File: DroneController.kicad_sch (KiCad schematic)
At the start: 36 parts, among them P1 USB_C_Plug, U2 TPS62152RGTR, U3 BMP280, U4 MPU-6500, U6 L86-M33, Y1 8Mhz

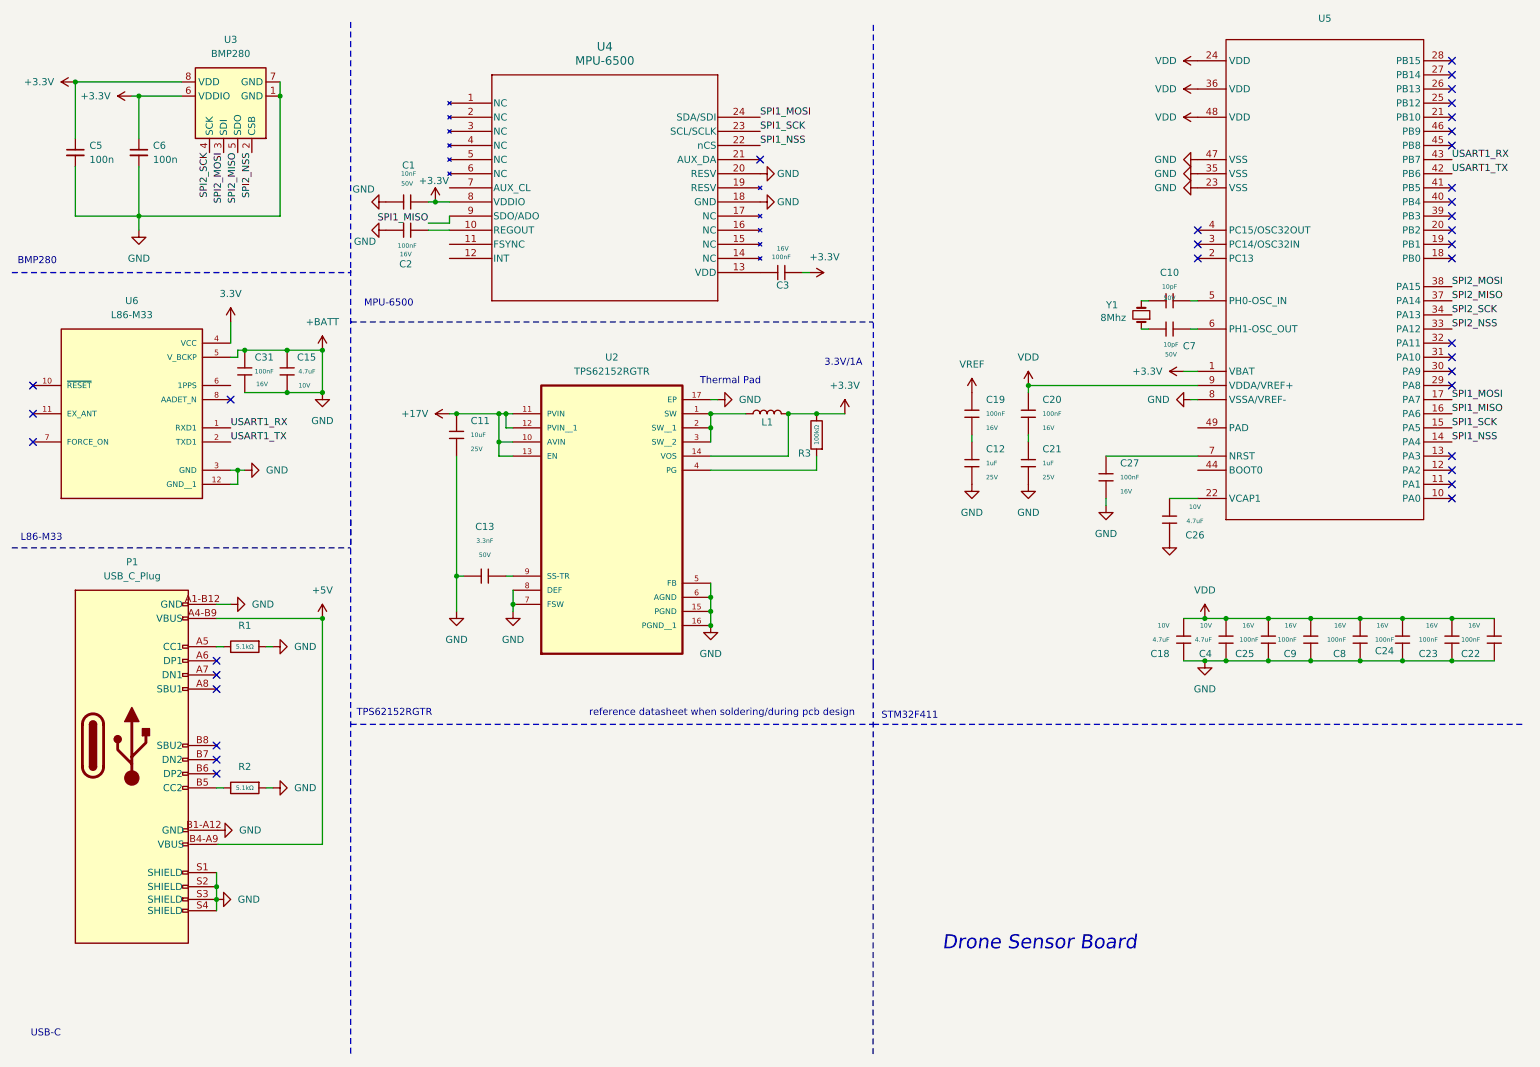
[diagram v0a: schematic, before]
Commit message: Started PCB Design
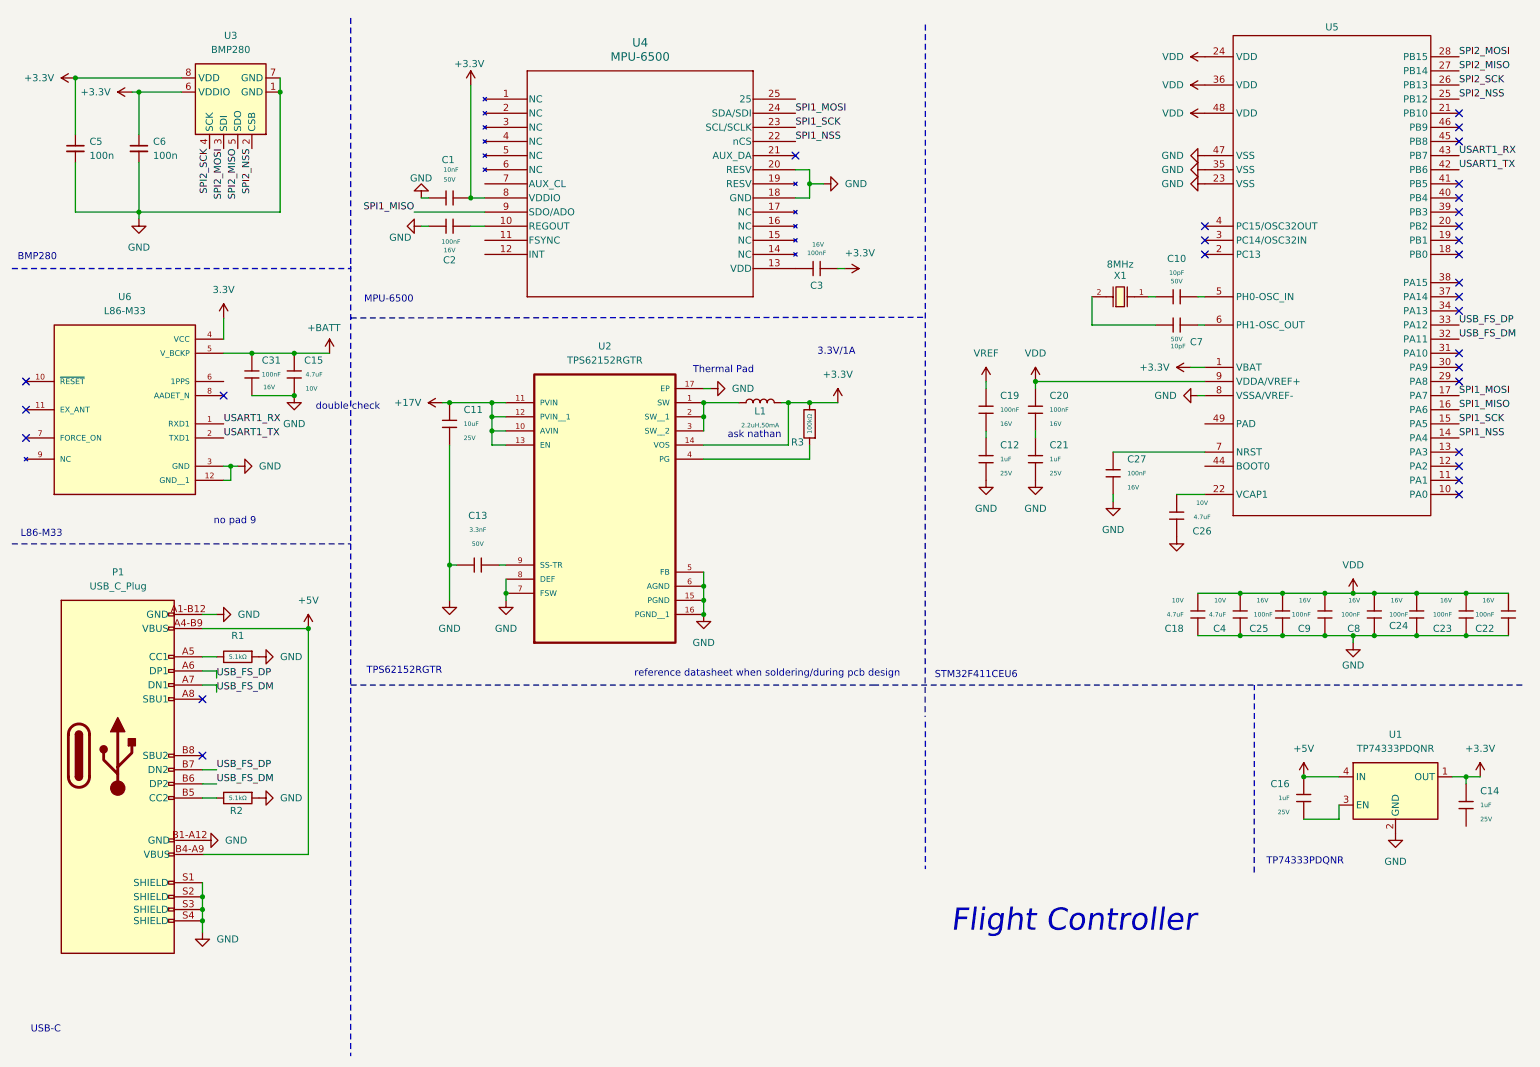
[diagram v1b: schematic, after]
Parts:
- removed Y1: 8Mhz, symbol Device:Crystal_Small
- added C14, C16: 1uF, PCM_JLCPCB:C_0402, symbol PCM_JLCPCB-Capacitors:0402,1uF
- added U1: TP74333PDQNR, Package_DFN_QFN:OnSemi_XDFN4-1EP_1.0x1.0mm_EP0.52x0.52mm, symbol Regulator_Linear:NCP115AMX250TCG
- added X1: X50328MSB2GI, PCM_JLCPCB:CRYSTAL-SMD_L5.0-W3.2, symbol PCM_JLCPCB-Crystals:Crystal, 8MHz, 20pF, ±10ppm
- P1: footprint (none) -> MC311D:USB-C-SMD_MC-311D
- U5: footprint ProLib_pcs_2025-03-31:UFQFPN-48_L7.0-W7.0-P0.50-BL-EP -> Package_DFN_QFN:QFN-48-1EP_7x7mm_P0.5mm_EP5.6x5.6mm
- U6: footprint L86-M33:XCVR_L86-M33 -> L86:XCVR_L86-M33
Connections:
- net +3.3V: now also C14.1, U1.1 (OUT)
- net +5V: now also C16.1, U1.4 (IN)
- net +BATT: no longer C1.1, C11.2, C12.2, C13.1, C15.2, C18.2, C2.1, C21.2, C22.1, C23.1, C24.1, C25.1, C26.2, C27.2, C31.2, C4.1, C5.2, C6.2, C8.1, C9.1, P1.A1-B12 (GND), P1.B1-A12 (GND), P1.S1 (SHIELD), P1.S2 (SHIELD), P1.S3 (SHIELD), P1.S4 (SHIELD), R1.1, R2.1, U2.15 (PGND), U2.16 (PGND__1), U2.17 (EP), U2.5 (FB), U2.6 (AGND), U2.7 (FSW), U2.8 (DEF), U3.1 (GND), U3.7 (GND), U4.18 (GND), U4.20 (RESV), U5.23 (VSS), U5.35 (VSS), U5.47 (VSS), U5.8 (VSSA/VREF-), U6.12 (GND__1), U6.3 (GND)
- net SPI2_MISO: now also U5.27 (PB14); no longer U5.37 (PA14)
- net SPI2_MOSI: now also U5.28 (PB15); no longer U5.38 (PA15)
- net SPI2_NSS: now also U5.25 (PB12); no longer U5.33 (PA12)
- net SPI2_SCK: now also U5.26 (PB13); no longer U5.34 (PA13)
- net USB_FS_DP: now reaches P1.A6 (DP1)
- net USB_FS_DP: now also P1.B7 (DN2), U5.33 (PA12)
- net USB_FS_DM: now reaches P1.A7 (DN1)
- net USB_FS_DM: now also P1.B6 (DP2), U5.32 (PA11)
- net at C7.2: now also X1.2
- net at C10.1: now also X1.1
- new net: C16.2, U1.3 (EN)
- new net GND: C1.1, C11.2, C12.2, C13.1, C15.2, C18.2, C2.1, C21.2, C22.1, C23.1, C24.1, C25.1, C26.2, C27.2, C31.2, C4.1, C5.2, C6.2, C8.1, C9.1, P1.A1-B12 (GND), P1.B1-A12 (GND), P1.S1 (SHIELD), P1.S2 (SHIELD), P1.S3 (SHIELD), P1.S4 (SHIELD), R1.1, R2.1, U1.2 (GND), U1.5 (GND), U2.15 (PGND), U2.16 (PGND__1), U2.17 (EP), U2.5 (FB), U2.6 (AGND), U2.7 (FSW), U2.8 (DEF), U3.1 (GND), U3.7 (GND), U4.18 (GND), U4.20 (RESV), U5.23 (VSS), U5.35 (VSS), U5.47 (VSS), U5.8 (VSSA/VREF-), U6.12 (GND__1), U6.3 (GND)
- no-connect marks 35 -> 29
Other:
- note added: "Flight Controller"
- note added: "STM32F411CEU6"
- note added: "TP74333PDQNR"
- note added: "ask nathan"
- note added: "double check"
- note added: "no pad 9"
- note removed: "Drone Sensor Board"
- note removed: "STM32F411"
- moved on the sheet: C1, C10, C11, C12, C13, C15, C18, C19, C2, C20, C21, C22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

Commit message: Updated STM32 and overhauled SPI wiring, added external flash memory, added LoRa Transciever, moved buck converter to ESC-Board which will handle power distrubution, signficant progress on PCB design.
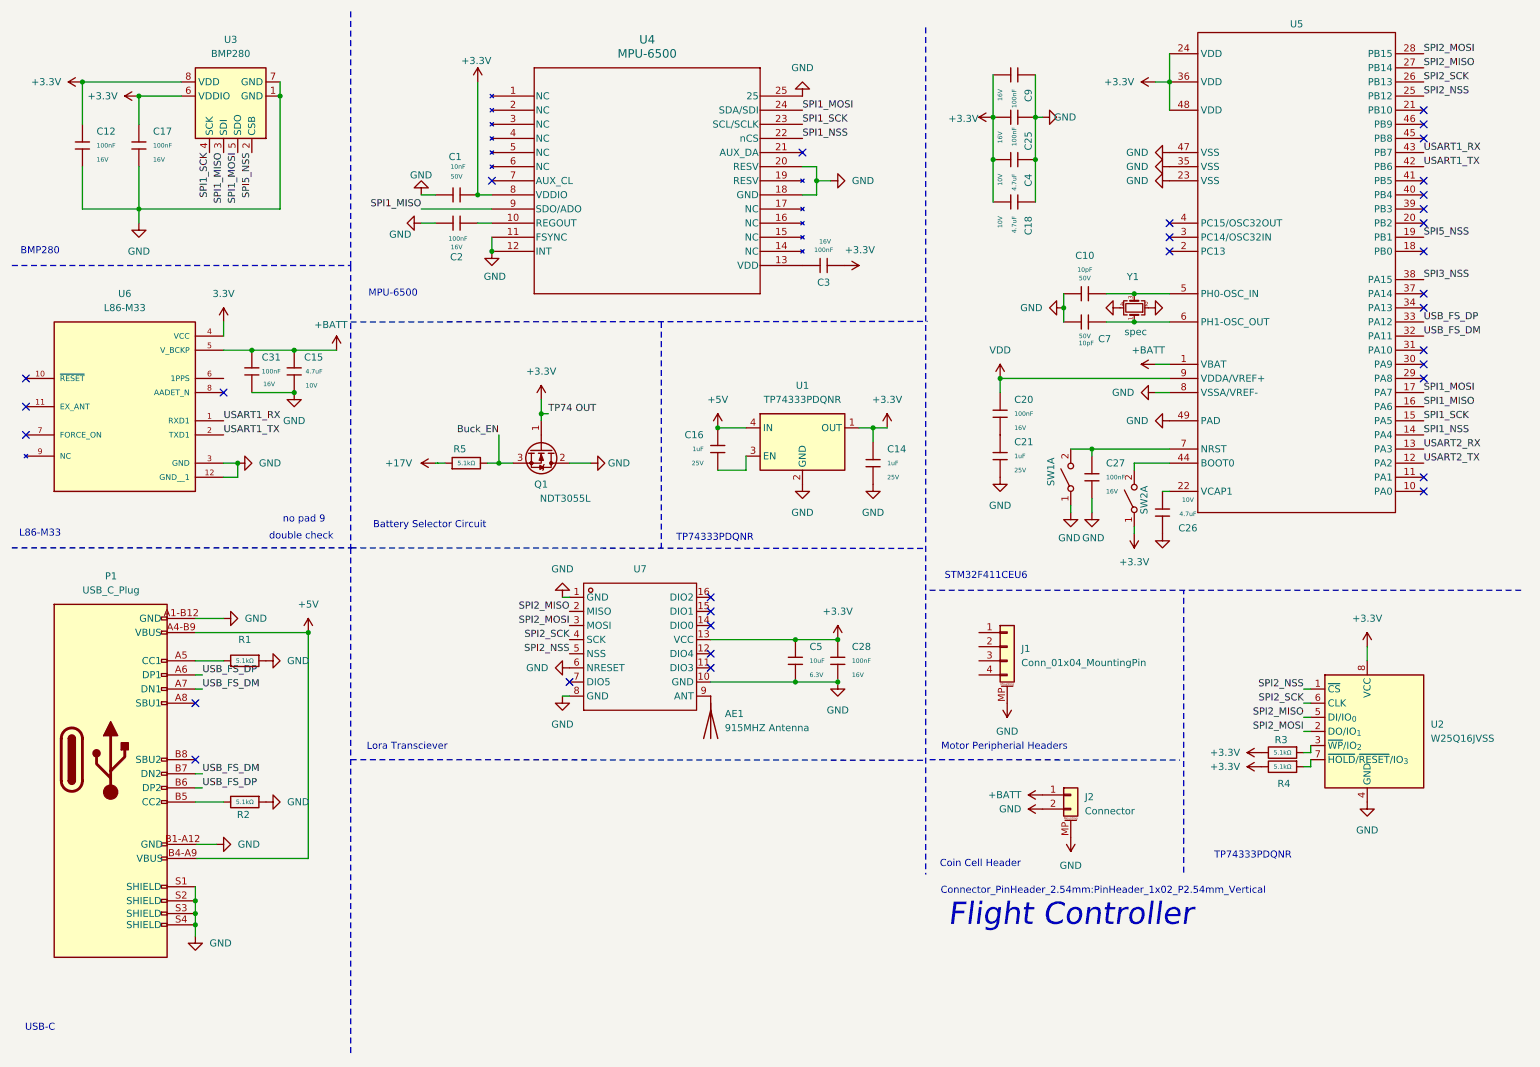
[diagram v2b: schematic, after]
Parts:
- removed C11: 10uF, PCM_JLCPCB:C_0603, symbol PCM_JLCPCB-Capacitors:0603,10uF,(2)
- removed C12: 1uF, PCM_JLCPCB:C_0402, symbol PCM_JLCPCB-Capacitors:0402,1uF
- removed C13: 3.3nF, PCM_JLCPCB:C_0402, symbol PCM_JLCPCB-Capacitors:0402,3.3nF
- removed C19, C22, C23, C24, C8: 100nF, PCM_JLCPCB:C_0402, symbol PCM_JLCPCB-Capacitors:0402,100nF
- removed C5, C6: 100n, symbol Device:C_Small
- removed L1: 2.2uH,50mA, PCM_JLCPCB:L_0805, symbol PCM_JLCPCB-Inductors:2.2uH,50mA
- removed R3: 100kΩ, PCM_JLCPCB:R_0402, symbol PCM_JLCPCB-Resistors:0402,100kΩ
- removed U2: TPS62152RGTR, TPS62152RGTR:QFN50P300X300X100-17N, symbol TPS62152RGTR:TPS62152RGTR
- removed X1: X50328MSB2GI, PCM_JLCPCB:CRYSTAL-SMD_L5.0-W3.2, symbol PCM_JLCPCB-Crystals:Crystal, 8MHz, 20pF, ±10ppm
- added AE1: 915MHZ Antenna, symbol Device:Antenna
- added C12, C17, C28: 100nF, PCM_JLCPCB:C_0402, symbol PCM_JLCPCB-Capacitors:0402,100nF
- added C5: 10uF, PCM_JLCPCB:C_0402, symbol PCM_JLCPCB-Capacitors:0402,10uF
- added J1: Conn_01x04_MountingPin, symbol Connector_Generic_MountingPin:Conn_01x04_MountingPin
- added J2: Connector, symbol Connector_Generic_MountingPin:Conn_01x02_MountingPin
- added Q1: NDT3055L, Package_TO_SOT_SMD:SOT-223-3_TabPin2, symbol Transistor_FET:NDT3055L
- added R3, R4, R5: 5.1kΩ, PCM_JLCPCB:R_0402, symbol PCM_JLCPCB-Resistors:0402,5.1kΩ
- added SW1, SW2: SW_DPST_x2, symbol Switch:SW_DPST_x2
- added U2: W25Q16JVSS, Package_SO:SOIC-8_5.3x5.3mm_P1.27mm, symbol Memory_Flash:W25Q16JVSS
- added U7: 915MHz, ProLib_pcs_2025-05-18:COMM-SMD_LORA1276-C1-915MHZ, symbol lora1276:LORA1276-C1-915MHZ
- added Y1: spec, symbol Device:Crystal_GND24_Small
- P1: footprint MC311D:USB-C-SMD_MC-311D -> USB-C:USB-C
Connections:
- net +17V: now also R5.1
- net +3.3V: now also C18.1, C25.2, C4.2, C9.2, U5.24 (VDD), U5.36 (VDD), U5.48 (VDD), C12.1, C17.1, C28.1, C5.1, Q1.1 (G), R3.2, R4.2, SW2.1 (A), U2.8 (VCC), U7.13 (VCC); no longer U5.1 (VBAT)
- net +BATT: now also U5.1 (VBAT), J2.1 (Pin_1)
- net GND: now also C10.1, C14.2, C7.2, U4.11 (FSYNC), U4.12 (INT), U4.25, U5.49 (PAD), C12.2, C17.2, C28.2, C5.2, J1.MP (MountPin), J2.2 (Pin_2), J2.MP (MountPin), Q1.2 (D), SW1.1 (A), U2.4 (GND), U7.1 (GND), U7.10 (GND), U7.6 (NRESET), U7.8 (GND), Y1.2, Y1.4
- net SPI1_MISO: now also U3.3 (SDI)
- net SPI1_MOSI: now also U3.5 (SDO)
- net SPI1_SCK: now also U3.4 (SCK)
- net SPI2_MISO: now also U2.5 (DI/IO_{0}), U7.2 (MISO); no longer U3.5 (SDO)
- net SPI2_MOSI: now also U2.2 (DO/IO_{1}), U7.3 (MOSI); no longer U3.3 (SDI)
- net SPI2_NSS: now also U2.1 (~{CS}), U7.5 (NSS); no longer U3.2 (CSB)
- net SPI2_SCK: now also U2.6 (CLK), U7.4 (SCK); no longer U3.4 (SCK)
- net USB_FS_DM: now also P1.B7 (DN2); no longer P1.B6 (DP2)
- net USB_FS_DP: now also P1.B6 (DP2); no longer P1.B7 (DN2)
- net VDD: no longer C18.1, C25.2, C4.2, C9.2, U5.24 (VDD), U5.36 (VDD), U5.48 (VDD)
- net USART2_TX: now reaches U5.12 (PA2)
- net USART2_RX: now reaches U5.13 (PA3)
- net SPI5_NSS: now reaches U5.19 (PB1)
- net SPI5_NSS: now also U3.2 (CSB)
- net SPI3_NSS: now reaches U5.38 (PA15)
- net at U5.44 (BOOT0): now also SW2.2 (B)
- net at C10.2, U5.5 (PH0-OSC_IN): now also Y1.3
- net at C7.1, U5.6 (PH1-OSC_OUT): now also Y1.1
- net at C27.1, U5.7 (NRST): now also SW1.2 (B)
- new net: R4.1, U2.7 (~{HOLD}/~{RESET}/IO_{3})
- new net: AE1.1 (A), U7.9 (ANT)
- new net: R3.1, U2.3 (~{WP}/IO_{2})
- new net Buck_EN: Q1.3 (S), R5.2
- no-connect marks 29 -> 32
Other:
- note added: "Battery Selector Circuit"
- note added: "Coin Cell Header"
- note added: "Connector_PinHeader_2.54mm:PinHeader_1x02_P2.54mm_Vertical"
- note added: "Lora Transciever"
- note added: "Motor Peripherial Headers"
- note removed: "3.3V/1A"
- note removed: "TPS62152RGTR"
- note removed: "Thermal Pad"
- note removed: "ask nathan"
- note removed: "reference datasheet when soldering/during pcb design"
- moved on the sheet: C1, C10, C14, C15, C16, C18, C2, C20, C21, C25, C26, C27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

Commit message: Finalized PCB Design
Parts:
- removed C14, C16: 1uF, PCM_JLCPCB:C_0402, symbol PCM_JLCPCB-Capacitors:0402,1uF
- removed C4: 4.7uF, PCM_JLCPCB:C_0402, symbol PCM_JLCPCB-Capacitors:0402,4.7uF
- removed J1: Conn_01x04_MountingPin, symbol Connector_Generic_MountingPin:Conn_01x04_MountingPin
- removed Q1: NDT3055L, Package_TO_SOT_SMD:SOT-223-3_TabPin2, symbol Transistor_FET:NDT3055L
- removed R5: 5.1kΩ, PCM_JLCPCB:R_0402, symbol PCM_JLCPCB-Resistors:0402,5.1kΩ
- removed SW1, SW2: SW_DPST_x2, symbol Switch:SW_DPST_x2
- removed U1: TP74333PDQNR, Package_DFN_QFN:OnSemi_XDFN4-1EP_1.0x1.0mm_EP0.52x0.52mm, symbol Regulator_Linear:NCP115AMX250TCG
- added C29: 100nF, PCM_JLCPCB:C_0402, symbol PCM_JLCPCB-Capacitors:0402,100nF
- added C6, C8: 10uF, PCM_JLCPCB:C_0402, symbol PCM_JLCPCB-Capacitors:0402,10uF
- added J1, J3: Connector, TerminalBlock:TerminalBlock_MaiXu_MX126-5.0-02P_1x02_P5.00mm, symbol Connector_Generic_MountingPin:Conn_01x02_MountingPin
- added SW1: SW_SPDT, Switches:SW-SMD_MSK12CO2, symbol Switch:SW_SPDT
- added U9: AP7361C-33E, Package_TO_SOT_SMD:SOT-223-3_TabPin2, symbol Regulator_Linear:AP7361C-33E
- AE1: footprint (none) -> Connector_Coaxial:SMA_BAT_Wireless_BWSMA-KWE-Z001; LCSC (none) -> C496551
- J2: footprint (none) -> TerminalBlock:TerminalBlock_MaiXu_MX126-5.0-02P_1x02_P5.00mm
- U7: footprint ProLib_pcs_2025-05-18:COMM-SMD_LORA1276-C1-915MHZ -> Lora1276:COMM-SMD_LORA1276-C1-915MHZ
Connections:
- net +3.3V: now also C29.2, C6.1, J3.1 (Pin_1), SW1.3 (C), U9.3 (VO)
- net +5V: now also C8.1, U9.1 (VI)
- net GND: now also U6.6 (1PPS), C29.1, C6.2, C8.2, J3.2 (Pin_2), SW1.1 (A), SW1.4, SW1.5, U9.2 (GND); no longer J2.MP (MountPin), U7.6 (NRESET)
- net SPI1_MISO: now also U2.5 (DI/IO_{0}), U7.2 (MISO); no longer U3.3 (SDI), U4.9 (SDO/ADO)
- net SPI1_MOSI: now also U2.2 (DO/IO_{1}), U7.3 (MOSI); no longer U3.5 (SDO), U4.24 (SDA/SDI)
- net SPI1_NSS: now also U7.5 (NSS); no longer U4.22 (nCS)
- net SPI1_SCK: now also U2.6 (CLK), U7.4 (SCK); no longer U3.4 (SCK), U4.23 (SCL/SCLK)
- net SPI2_MISO: now also U4.9 (SDO/ADO); no longer U2.5 (DI/IO_{0}), U7.2 (MISO)
- net SPI2_MOSI: now also U4.24 (SDA/SDI); no longer U2.2 (DO/IO_{1}), U7.3 (MOSI)
- net SPI2_NSS: now also U4.22 (nCS); no longer U2.1 (~{CS}), U7.5 (NSS)
- net SPI2_SCK: now also U4.23 (SCL/SCLK); no longer U2.6 (CLK), U7.4 (SCK)
- net SPI3_NSS: now also U3.2 (CSB)
- net SPI5_NSS: now also U2.1 (~{CS}); no longer U3.2 (CSB)
- net USART2_RX: now also J1.1 (Pin_1)
- net USART2_TX: now also J1.2 (Pin_2)
- net SPI5_SCK: now reaches U5.18 (PB0)
- net Lora_RES: now reaches U5.20 (PB2)
- net Lora_RES: now also U7.6 (NRESET)
- net SPI3_SCK: now reaches U5.39 (PB3)
- net SPI3_SCK: now also U3.4 (SCK)
- net SPI3_MISO: now reaches U5.40 (PB4)
- net SPI3_MISO: now also U3.3 (SDI)
- net SPI3_MOSI: now reaches U5.41 (PB5)
- net SPI3_MOSI: now also U3.5 (SDO)
- net at U5.44 (BOOT0): now also SW1.2 (B)
- no-connect marks 32 -> 27
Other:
- note added: "AP7361C-33E"
- note added: "Alternate Power Source"
- note added: "BAROMETER"
- note added: "FIXED LEVEL SHIFTEER"
- note added: "FLASH MEMORY"
- note added: "GNSS"
- note added: "IMU"
- note added: "LORA 1276"
- note added: "MC-311D"
- note added: "MCU"
- note added: "STM32 Capacitors"
- note added: "TRANSCIEVER"
- note added: "UART Peripheral"
- note removed: "Battery Selector Circuit"
- note removed: "Connector_PinHeader_2.54mm:PinHeader_1x02_P2.54mm_Vertical"
- note removed: "Lora Transciever"
- note removed: "Motor Peripherial Headers"
- moved on the sheet: C18, C25, C26, C27, C9, R3, R4, U2
